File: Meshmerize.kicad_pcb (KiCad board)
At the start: 2 copper layers, 113.9 x 108.8 mm, 52 parts, among them J1 Conn_01x19_Male, J2 Conn_01x19_Male, J3 Conn_01x04_Female, M1 Motor_DC, M2 Motor_DC, U1 LM324, U2 ESP32-DEVKITC-32D, U3 TCRT5000, U4 TCRT5000, U5 MT3608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

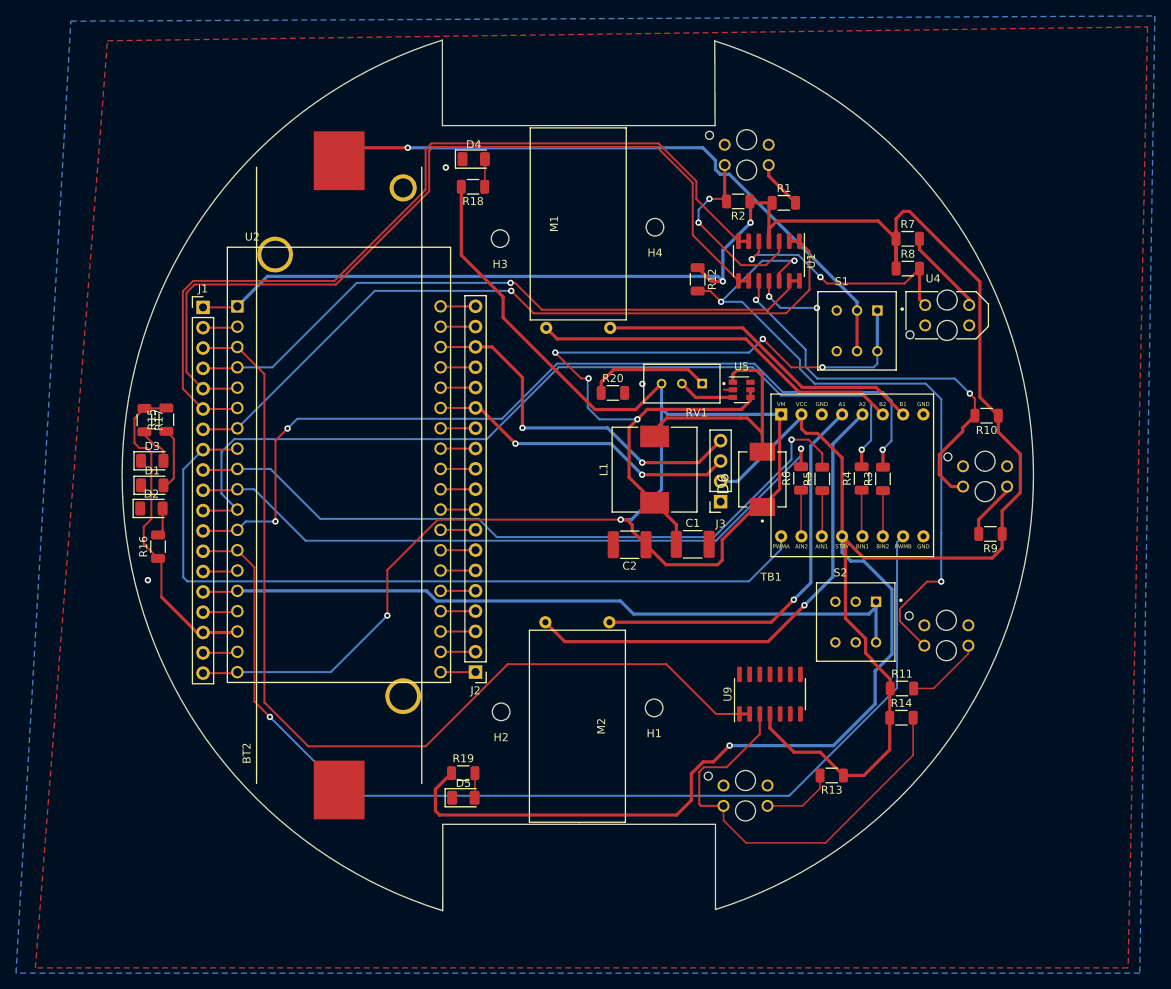
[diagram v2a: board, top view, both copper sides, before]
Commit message: Optimized schematics, routing and performed clean up
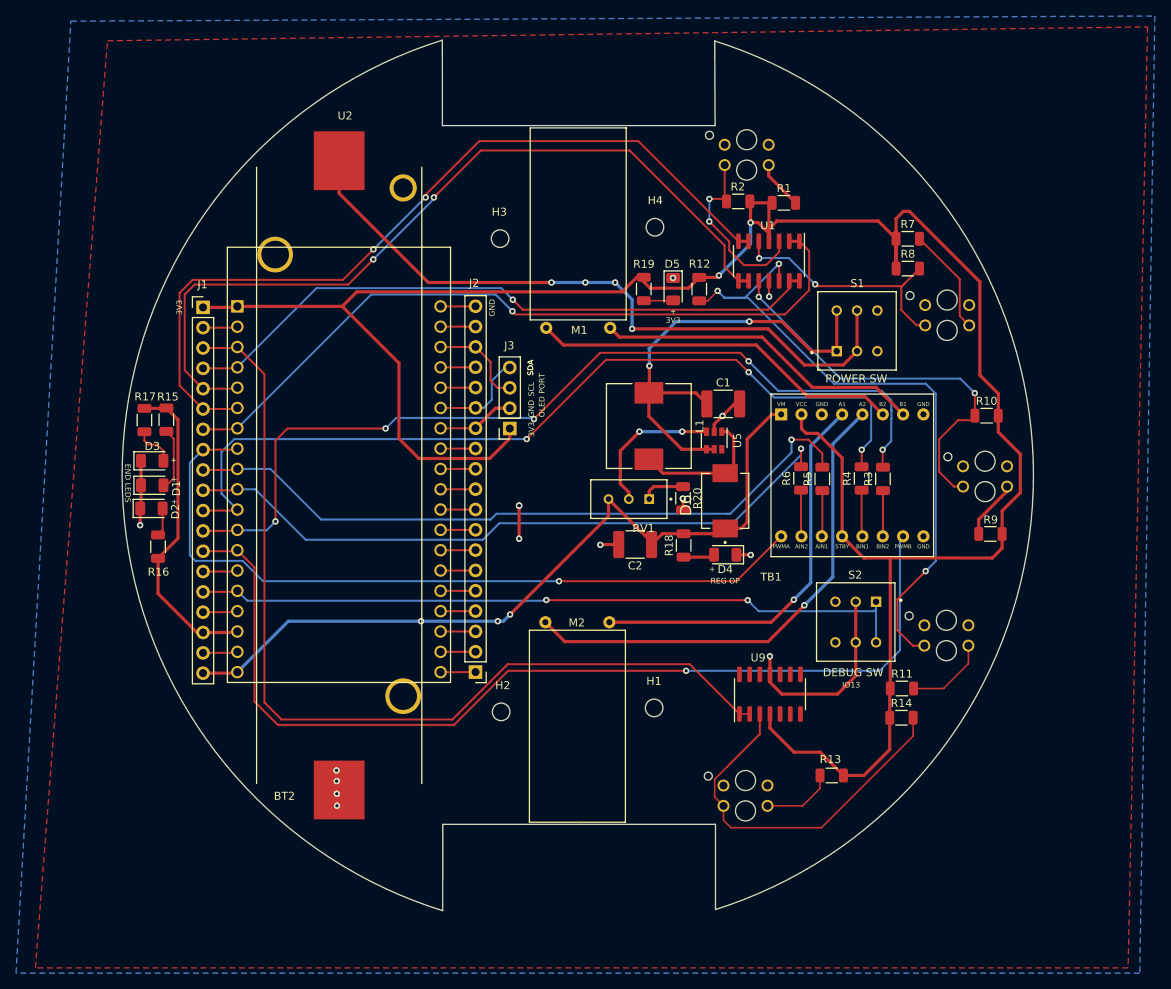
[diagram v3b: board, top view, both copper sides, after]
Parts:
- U4: moved to B.Cu
- moved D5 68.8 mm to (163.0, 68.2), turned to 270 degrees
- moved R19 64.6 mm to (159.3, 68.1), turned to 270 degrees
- moved D4 58.6 mm to (169.5, 101.4), turned to 180 degrees
- moved R18 52.0 mm to (164.3, 100.2), turned to 90 degrees
- moved J3 27.9 mm to (142.5, 85.6)
- moved C1 18.0 mm to (169.2, 82.5)
- moved RV1 15.9 mm to (157.4, 94.4)
- moved R20 15.8 mm to (164.2, 94.3), turned to 270 degrees
- moved U5 7.21 mm to (168.1, 87.1), turned to 270 degrees
- moved L1 5.49 mm to (159.9, 85.3), turned to 270 degrees
- moved D6 5.37 mm to (169.5, 94.6)
- moved R12 1.24 mm to (166.2, 68.1)
- moved C2 0.69 mm to (158.2, 100.1)
- turned S1 to 180 degrees
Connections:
- J2 pad 14: SCL_OLED -> SDA_OLED
- J2 pad 17: SDA_OLED -> SCL_OLED
- J3 pad 1: GND -> 3V3
- J3 pad 2: 3V3 -> GND
- S1 pad 3: (no net) -> Net-(S1-Pad3)
- S1 pad 6: (no net) -> Net-(S1-Pad6)
- S2 pad 3: (no net) -> Net-(S2-Pad3)
- S2 pad 6: (no net) -> Net-(S2-Pad6)
- U2 pad 22: SDA_OLED -> SCL_OLED
- U2 pad 25: SCL_OLED -> SDA_OLED
- U5 pad 6: (no net) -> Net-(U5-Pad6)
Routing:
- net +V: track 181.0 -> 98.2 mm, vias 2 -> 3
- net 3V3: track 367.6 -> 292.4 mm, vias 3 -> 2
- net GND: track 22.8 -> 68.2 mm, vias 5 -> 15
- net SWO: track 100.2 -> 57.6 mm, vias 5 -> 2
- net SDA_OLED: track 45.8 -> 12.6 mm, vias 2 -> 0
- net SCL_OLED: track 39.2 -> 12.2 mm, vias 2 -> 0
- net Net-(D6-PadA): track 30.6 -> 16.9 mm
- net Net-(RV1-Pad2): track 7.08 -> 18.3 mm, vias 0 -> 2
- net PWMB: track 134.2 -> 124.3 mm
- net Net-(R20-Pad1): track 15.3 -> 5.47 mm
- net An5: track 55.1 -> 47.2 mm
- net SW: track 80.2 -> 85.6 mm, vias 1 -> 4
- net D3: track 108.7 -> 103.4 mm, vias 0 -> 2
- net An4: track 86.8 -> 82.0 mm
- net PWMA: track 99.5 -> 95.8 mm, vias 0 -> 1
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- added copper zone on F.Cu, net (none)
- removed copper zone on F.Cu, net GND
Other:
- board text added: "+"
- board text added: "+ 3V3"
- board text added: "3V3"
- board text added: "DEBUG SW"
- board text added: "END LEDS"
- board text added: "GND"
- board text added: "IO13"
- board text added: "OLED PORT"
- board text added: "POWER SW"
- board text added: "REG OP"
- board text added: "SCL"
- board text added: "SDA"

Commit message: Added R-Pot for LSA sensitivity, jumper to power ESP32 using inbuilt regulator, minor optimizations
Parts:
- added G***: LOGO, SRA_Logo:sralogo, B.Cu at (152.2, 78.4)
- added G***: LOGO, SRA_Logo:sralogo, F.Cu at (185.3, 54.9)
- added JP1: SolderJumper_2_Open, Jumper:SolderJumper-2_P1.3mm_Open_Pad1.0x1.5mm, B.Cu at (115.9, 116.0)
- added REF**: KiCad-Logo2_8mm_SilkScreen, Symbol:KiCad-Logo2_8mm_SilkScreen, B.Cu at (154.0, 101.1)
- added REF**: OSHW-Logo2_14.6x12mm_SilkScreen, Symbol:OSHW-Logo2_14.6x12mm_SilkScreen, B.Cu at (151.2, 121.9)
- added RV2: R_POT, 3296W-1-202LF:TRIM_3296W-1-202LF, F.Cu at (185.7, 63.6)
- moved R7 1.54 mm to (193.8, 61.9)
- moved R8 1.54 mm to (193.8, 65.6)
- turned U5 to 90 degrees
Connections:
- J1 pad 19: +V -> Vin_ESP
- U1 pad 13: D4 -> POT_CON
- U1 pad 2: D1 -> POT_CON
- U1 pad 6: D2 -> POT_CON
- U1 pad 9: D3 -> POT_CON
- U2 pad 19: +V -> Vin_ESP
- U9 pad 2: D5 -> POT_CON
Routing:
- net POT_CON: track 0.00 -> 107.3 mm, vias 0 -> 2
- net +V: track 98.2 -> 86.4 mm
- net Vin_ESP: track 0.00 -> 11.1 mm
- net SWO: track 57.6 -> 49.6 mm
- net An1: track 23.4 -> 18.5 mm
- net 3V3: track 292.4 -> 288.1 mm
- net Net-(RV1-Pad2): track 18.3 -> 20.4 mm, vias 2 -> 0
- net Net-(D6-PadA): track 16.9 -> 15.4 mm
- net D5: track 117.1 -> 115.9 mm
- net D3: track 103.4 -> 102.2 mm
- net D2: track 104.4 -> 103.2 mm
- net D1: track 92.9 -> 91.7 mm
- net An2: track 31.8 -> 32.8 mm
- net GND: track 68.2 -> 67.4 mm, vias 15 -> 16
- net Net-(R7-Pad2): track 13.4 -> 14.1 mm, vias 0 -> 2
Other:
- board text added: "Short to Power ESP32 using onboard Regulator"
- board text added: "Society of Robotics and Automation SRA - VJTI"

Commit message: Modified Silkscreen and created Gerber Files
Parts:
- moved H4 1.59 mm to (159.9, 61.8)
- moved H1 1.00 mm to (159.7, 121.0)
- moved H3 0.99 mm to (142.3, 61.8)
- moved H2 0.78 mm to (142.2, 121.0)
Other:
- board text added: "+VBAT"
- board text added: "-VBAT"
- board text added: "0"
- board text added: "12"
- board text added: "13"
- board text added: "14"
- board text added: "15"
- board text added: "16"
- board text added: "17"
- board text added: "18"
- board text added: "19"
- board text added: "2"
- board text added: "21"
- board text added: "22"
- board text added: "23"
- board text added: "25"
- board text added: "26"
- board text added: "27"
- board text added: "32"
- board text added: "33"
- board text added: "34"
- board text added: "35"
- board text added: "4"
- board text added: "5"
- board text added: "CLK"
- board text added: "CMD"
- board text added: "D0"
- board text added: "D1"
- board text added: "D2"
- board text added: "D3"
- board text added: "EN"
- board text added: "IR1"
- board text added: "IR2"
- board text added: "IR3"
- board text added: "IR4"
- board text added: "IR5"
- board text added: "Keep Voltage under 6V"
- board text added: "MAZEBLAZE"
- board text added: "N20 6V 600 RPM"
- board text added: "RX"
- board text added: "TB6612FNG"
- board text added: "TX"
- board text added: "VADJ"
- board text added: "VIN"
- board text added: "VN"
- board text added: "VP"

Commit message: Made minor changes in Back silkscreen and front copper traces
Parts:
- moved REF** 50.0 mm to (122.5, 62.3), turned to 90 degrees
- moved REF** 29.4 mm to (121.9, 124.9), turned to 90 degrees
- moved G*** 16.9 mm to (161.9, 92.2), turned to 90 degrees
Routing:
- net Net-(RV1-Pad2): track 20.4 -> 22.3 mm, vias 0 -> 1

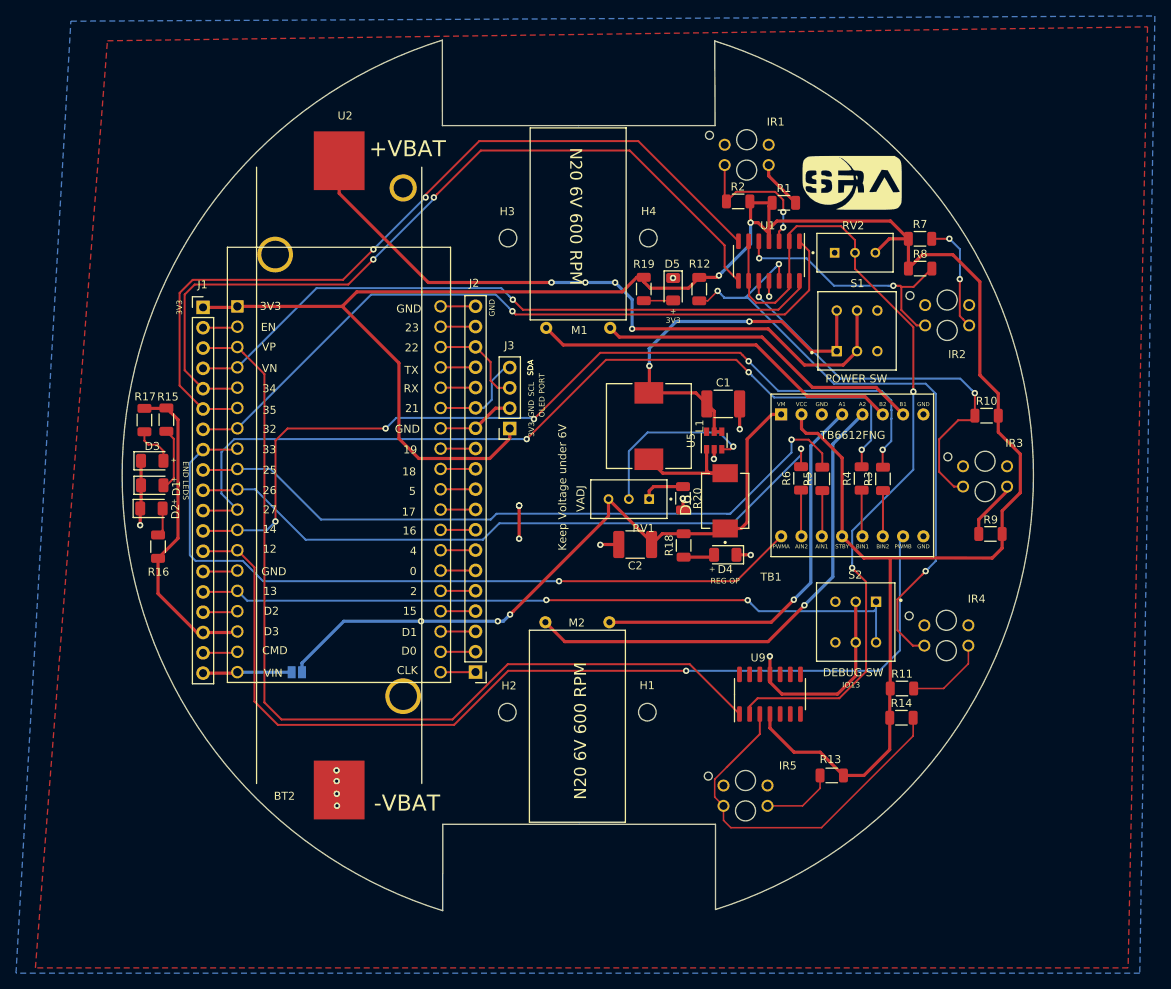
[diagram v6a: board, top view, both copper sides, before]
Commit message: Stitched Vias for Continuous Ground Plane, minor silkscreen fixes
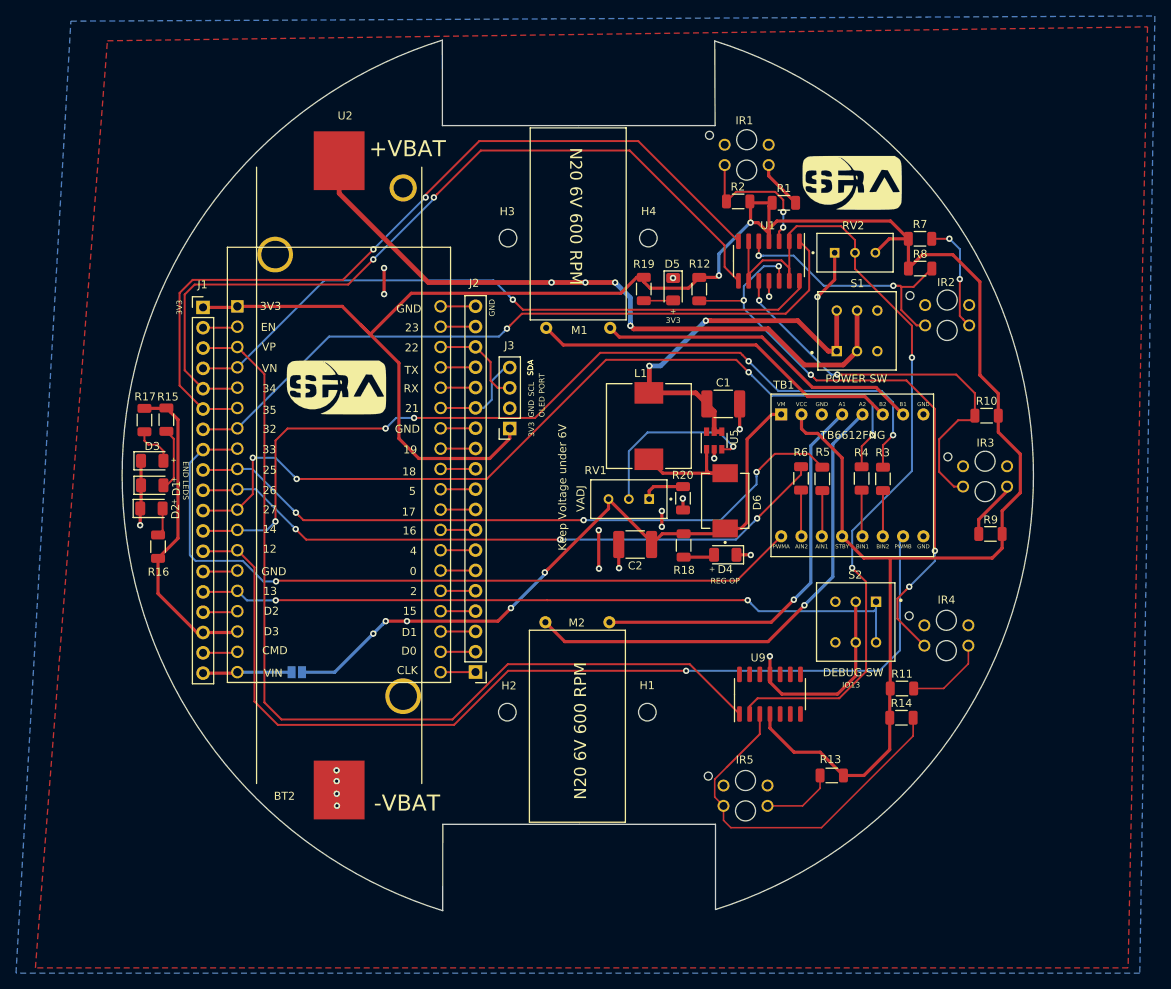
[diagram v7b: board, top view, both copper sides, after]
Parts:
- added G***: LOGO, SRA_Logo:sralogo, F.Cu at (120.8, 80.4)
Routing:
- net GND: track 67.4 -> 75.0 mm, vias 16 -> 20
- net An4: track 81.9 -> 77.7 mm, vias 3 -> 5
- net A2: track 84.8 -> 81.8 mm, vias 1 -> 3
- net A1: track 88.0 -> 85.1 mm, vias 1 -> 3
- net D1: track 91.7 -> 89.6 mm
- net B1: track 109.1 -> 107.1 mm, vias 3 -> 4
- net SWO: track 49.6 -> 48.4 mm
- net +V: track 86.4 -> 85.3 mm, vias 3 -> 5
- net D4: track 81.9 -> 82.7 mm

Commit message: Added 3D Files
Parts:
- removed G*** (x3): LOGO, SRA_Logo:sralogo
- removed REF**: KiCad-Logo2_8mm_SilkScreen, Symbol:KiCad-Logo2_8mm_SilkScreen
- removed REF**: OSHW-Logo2_14.6x12mm_SilkScreen, Symbol:OSHW-Logo2_14.6x12mm_SilkScreen
- C1, C2: footprint Capacitor_SMD:C_1812_4532Metric -> Capacitor_SMD:C_0805_2012Metric
- L1: footprint Inductor_SMD:L_10.4x10.4_H4.8 -> Inductor_SMD:L_12x12mm_H6mm
- moved D6 1.32 mm to (170.8, 94.8)
- moved RV1 1.16 mm to (157.4, 95.6)
- moved R20 0.64 mm to (164.3, 94.9)
- moved U5 0.57 mm to (168.6, 86.9)
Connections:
- S1 pad 3: Net-(S1-Pad3) -> (no net)
- S1 pad 6: Net-(S1-Pad6) -> (no net)
- S2 pad 3: Net-(S2-Pad3) -> (no net)
- S2 pad 6: Net-(S2-Pad6) -> (no net)
- U5 pad 6: Net-(U5-Pad6) -> (no net)
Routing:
- net Net-(RV1-Pad2): track 22.3 -> 24.0 mm
- net GND: track 75.0 -> 76.6 mm
- net Net-(R20-Pad1): track 5.47 -> 6.95 mm
- net SWO: track 48.4 -> 49.9 mm
- net +V: track 85.3 -> 86.4 mm
- net A1: track 85.1 -> 84.2 mm
